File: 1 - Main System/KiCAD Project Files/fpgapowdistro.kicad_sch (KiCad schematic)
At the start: 41 parts, among them Q4 2N7002, U1 MAX20029BATIA/V+, U30 STTH1002CB-TR

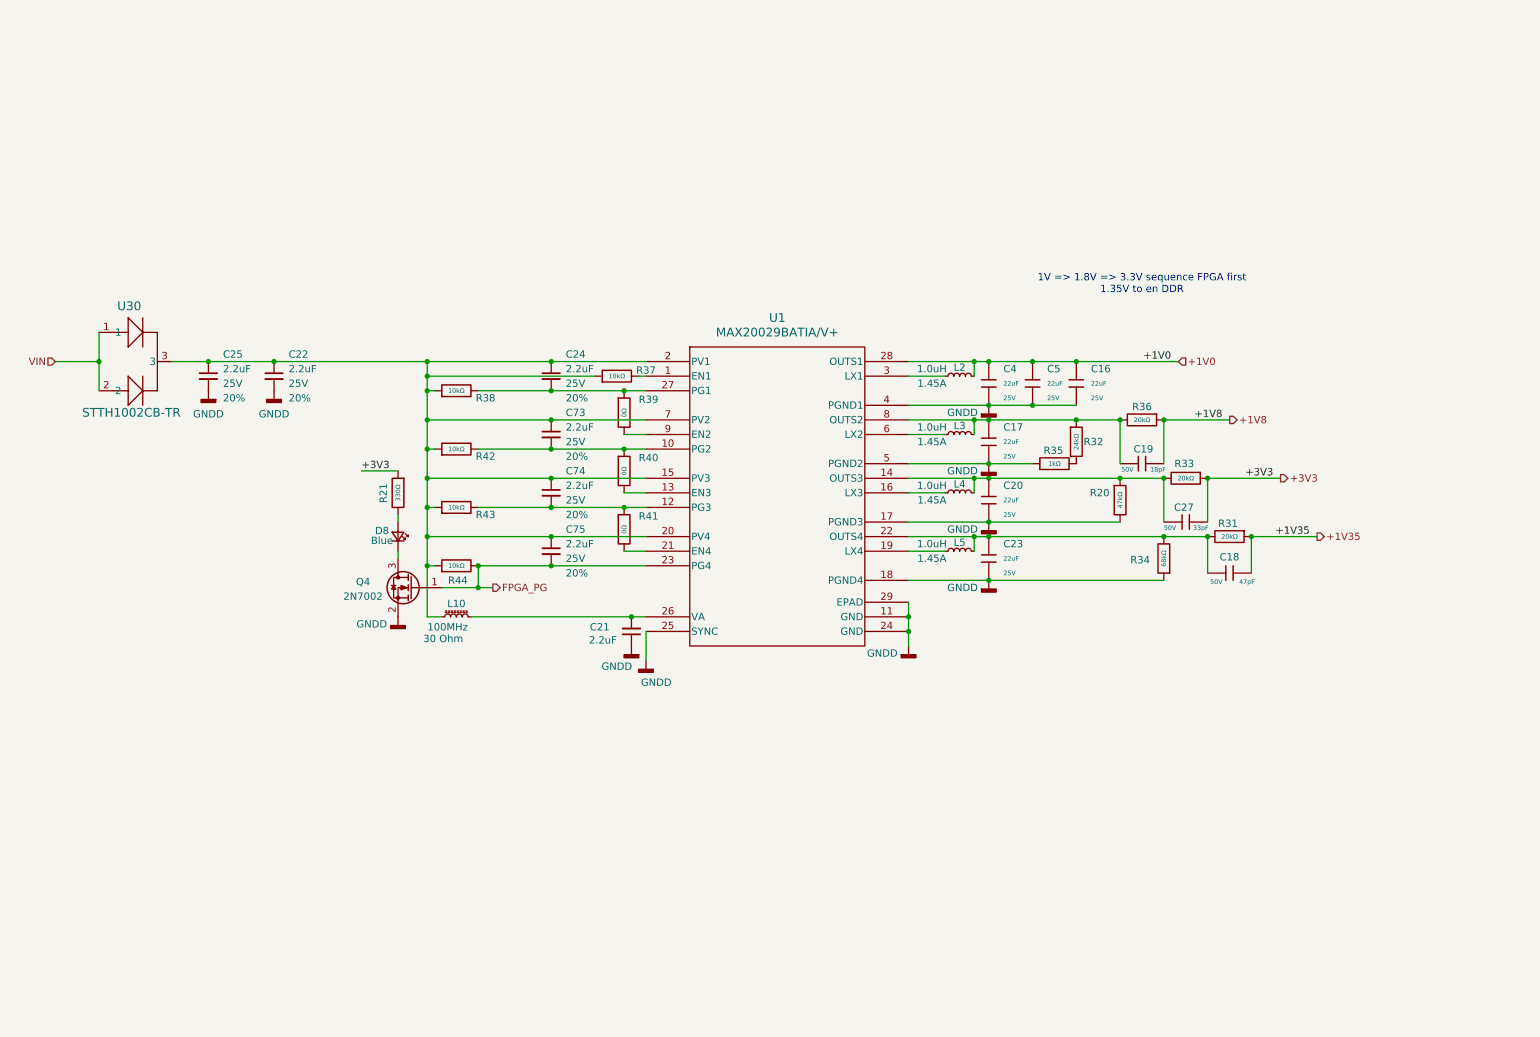
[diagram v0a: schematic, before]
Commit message: Routing DDR3 Completed (pre-review)
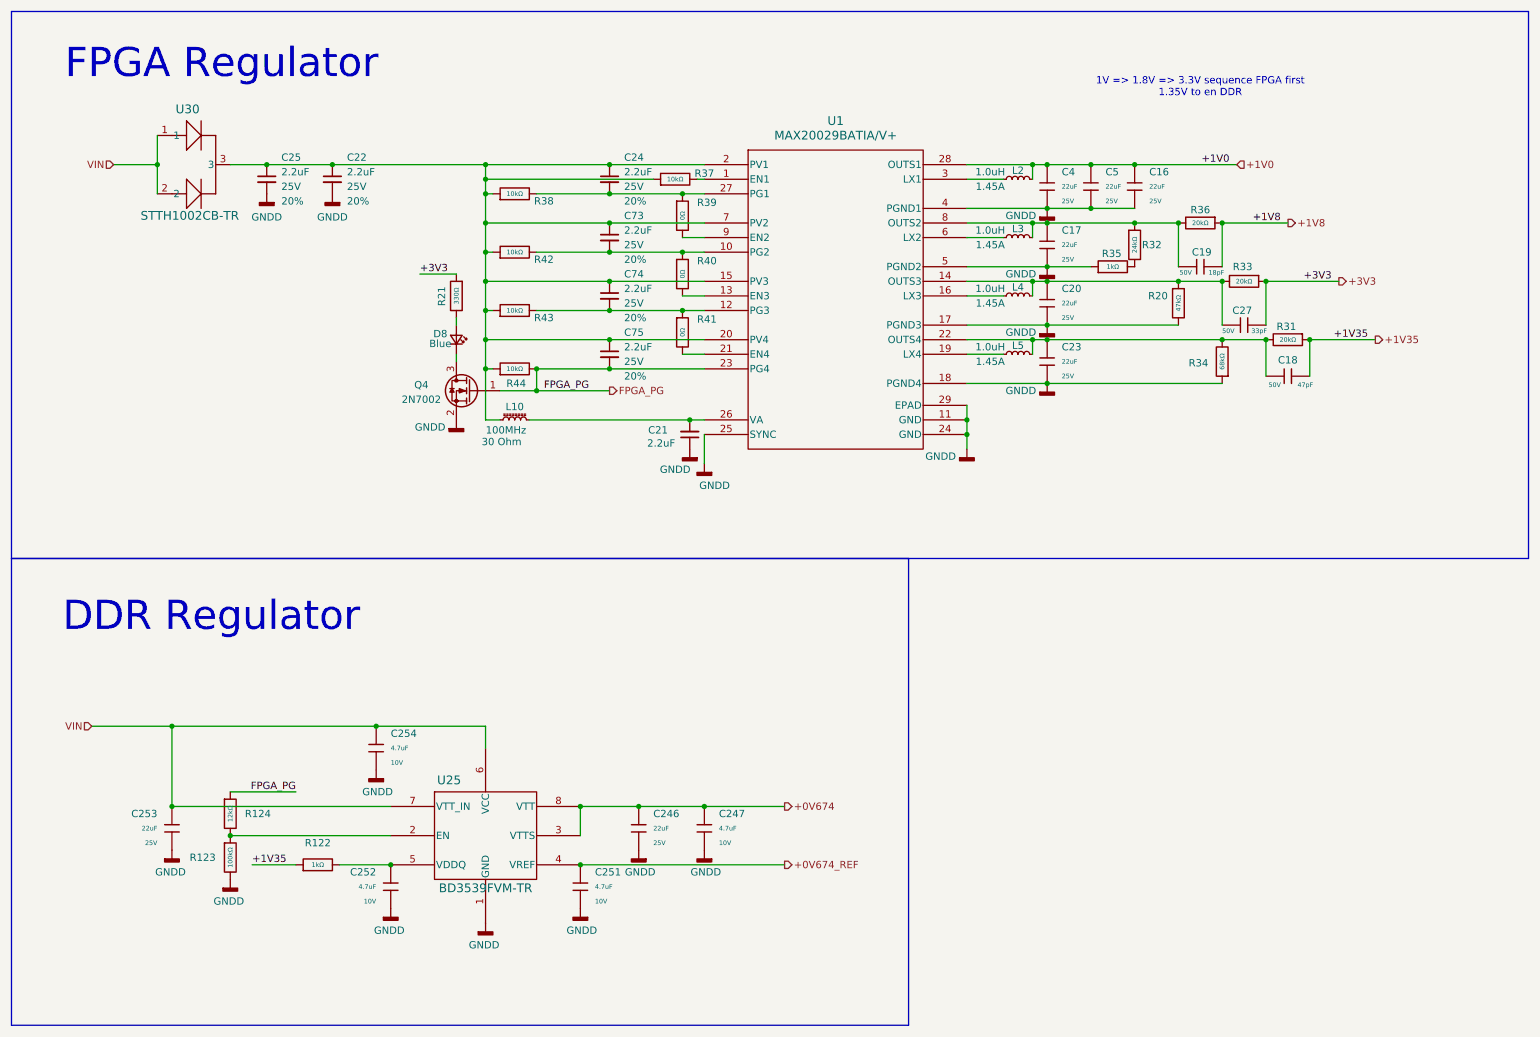
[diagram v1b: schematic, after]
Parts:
- added C246, C253: 22uF, PCM_JLCPCB:C_0805, symbol PCM_JLCPCB-Capacitors:0805,22uF
- added C247, C251, C252, C254: 4.7uF, PCM_JLCPCB:C_0805, symbol PCM_JLCPCB-Capacitors:0402,4.7uF
- added R122: 1kΩ, PCM_JLCPCB:R_0402, symbol PCM_JLCPCB-Resistors:0402,1kΩ
- added R123: 100kΩ, PCM_JLCPCB:R_0402, symbol PCM_JLCPCB-Resistors:0402,100kΩ
- added R124: 12kΩ, PCM_JLCPCB:R_0402, symbol PCM_JLCPCB-Resistors:0402,12kΩ
- added U25: BD3539FVM-TR, MSOP8_ROM, symbol libby:BD3539FVM-TR
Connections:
- net +1V35: now also R122.1
- net FPGA_PG: now also R124.1
- net GNDD: now also C246.2, C247.2, C251.2, C252.2, C253.2, C254.2, R123.2, U25.1 (GND)
- net VIN: now also C253.1, C254.1, U25.6 (VCC), U25.7 (VTT_IN)
- new net: R123.1, R124.2, U25.2 (EN)
- new net: C252.1, R122.2, U25.5 (VDDQ)
- new net +0V674: C246.1, C247.1, U25.3 (VTTS), U25.8 (VTT)
- new net +0V674_REF: C251.1, U25.4 (VREF)
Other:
- note added: "DDR Regulator"
- note added: "FPGA Regulator"
- moved on the sheet: C16, C17, C18, C19, C20, C21, C22, C23, C24, C25, C27, C4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
